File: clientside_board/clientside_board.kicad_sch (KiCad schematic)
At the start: 10 parts, among them J10 Comm Status LED, J11 12V Power Input, J2 USB_B, J4 UART Screw Terminal

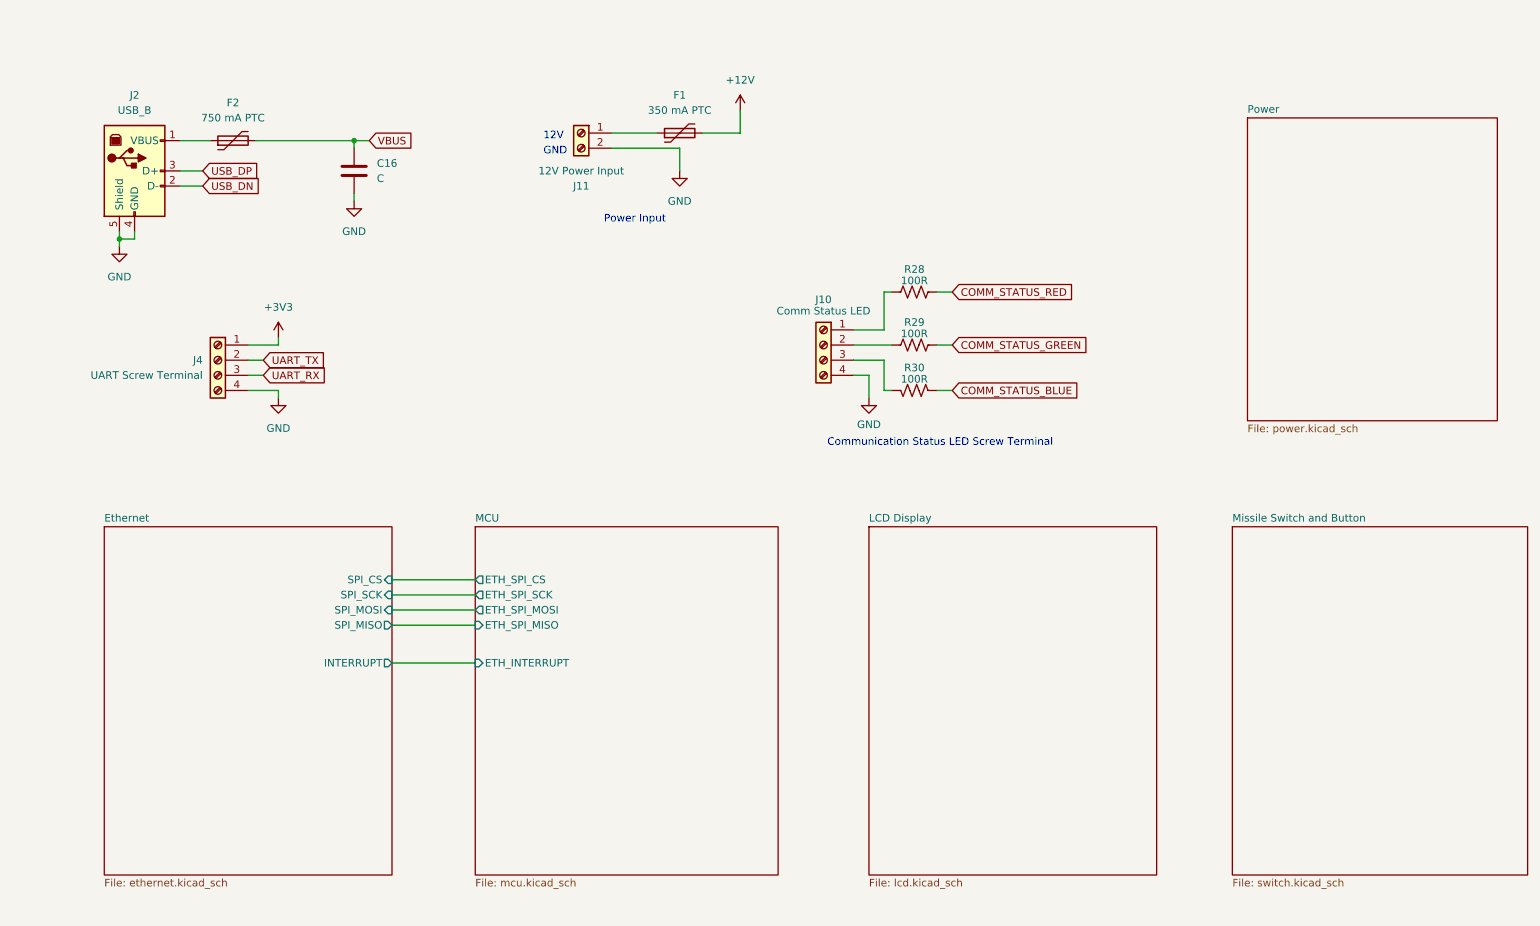
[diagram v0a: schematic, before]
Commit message: Cleanup Power and Ethernet Sheet
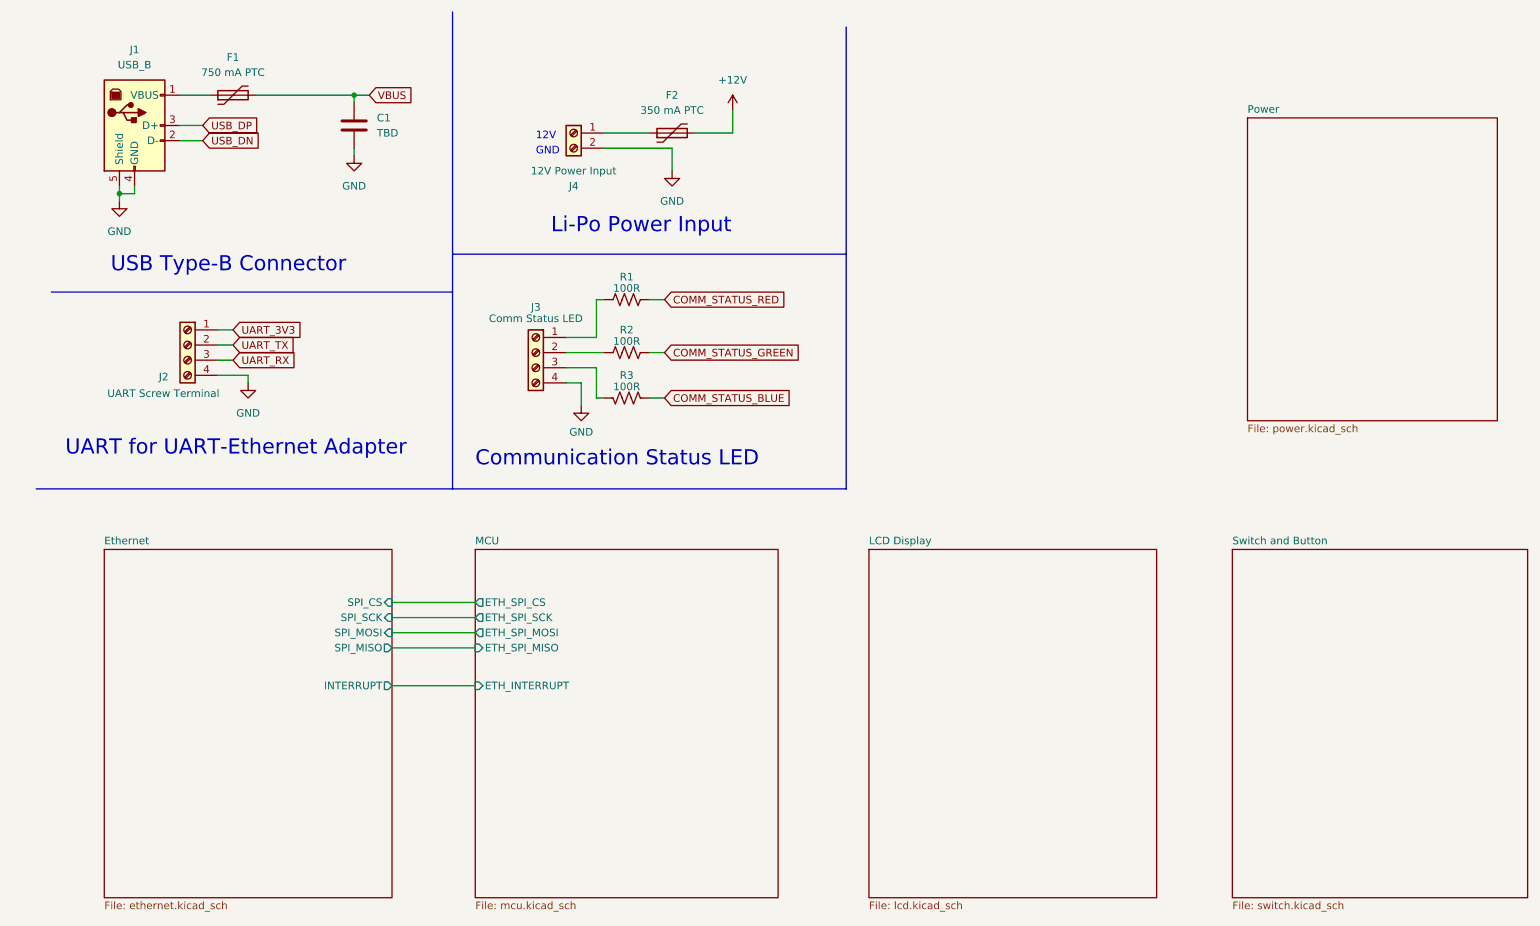
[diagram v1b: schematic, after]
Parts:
- C1: renamed from C16; value C -> TBD; footprint (none) -> Capacitor_SMD:C_0805_2012Metric_Pad1.18x1.45mm_HandSolder
- renumbered F2 to F1, F1 to F2, J2 to J1, J4 to J2, J10 to J3, J11 to J4, R28 to R1, R29 to R2, R30 to R3
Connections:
- net +3V3 renamed UART_3V3
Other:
- sheet Missile Switch and Button renamed Switch and Button
- note added: "Communication Status LED"
- note added: "Li-Po Power Input"
- note added: "UART for UART-Ethernet Adapter"
- note added: "USB Type-B Connector"
- note removed: "Communication Status LED Screw Terminal"
- note removed: "Power Input"
- title: (none) -> Top level connection and connectors
- moved on the sheet: C1, F1, F2, J1, J2, J3, J4, R1, R2, R3

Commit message: Start MCU pin connection
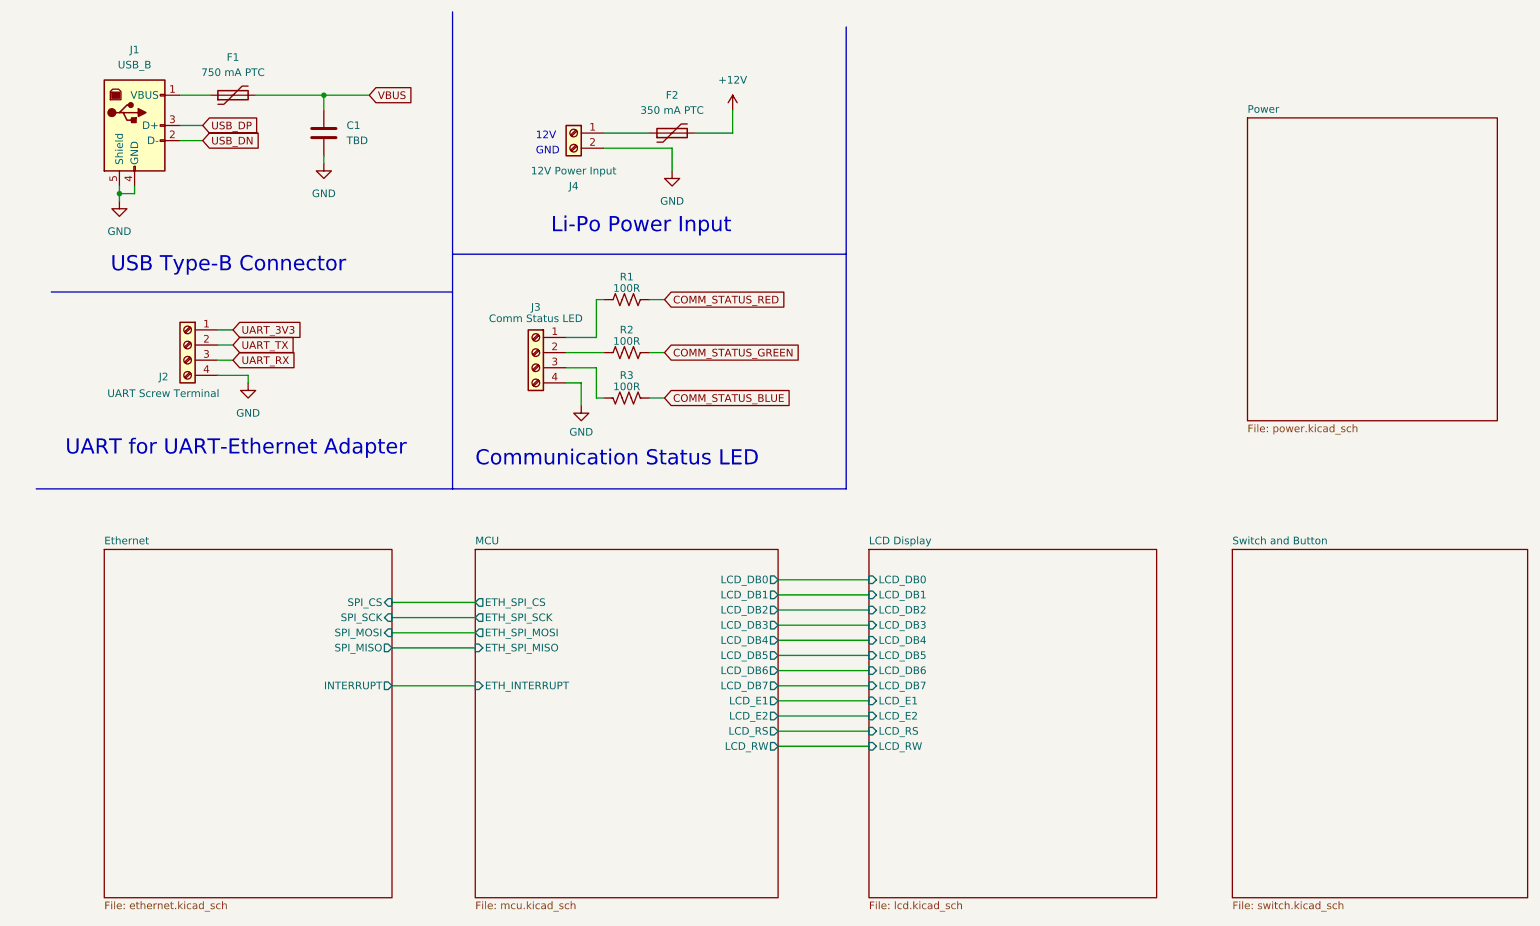
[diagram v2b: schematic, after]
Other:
- sheet LCD Display ports: added LCD_DB0, LCD_DB1, LCD_DB2, LCD_DB3, LCD_DB4, LCD_DB5, LCD_DB6, LCD_DB7, LCD_E1, LCD_E2, LCD_RS, LCD_RW; removed none
- sheet MCU ports: added LCD_DB0, LCD_DB1, LCD_DB2, LCD_DB3, LCD_DB4, LCD_DB5, LCD_DB6, LCD_DB7, LCD_E1, LCD_E2, LCD_RS, LCD_RW; removed none
- moved on the sheet: C1

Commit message: Update power for 5V LCD display
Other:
- sheet Power renamed 3V3 Power
- added sheet 5V Power (5v_power.kicad_sch)
- sheet 3V3 Power: file power.kicad_sch -> 3v3_power.kicad_sch
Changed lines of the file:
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@@
 	)
 	(sheet
-		(at 218.44 30.48)
+		(at 163.83 31.75)
 		(size 41.91 50.8)
 		(exclude_from_sim no)
@@
 			(color 0 0 0 0.0000)
 		)
-		(property "Sheetname" "Power"
-			(at 218.44 29.7684 0)
+		(property "Sheetname" "3V3 Power"
+			(at 163.83 31.0384 0)
 			(effects
 				(font
@@
 			)
 		)
-		(property "Sheetfile" "power.kicad_sch"
-			(at 218.44 81.8646 0)
+		(property "Sheetfile" "3v3_power.kicad_sch"
+			(at 163.83 83.1346 0)
 			(effects
 				(font
@@
 				)
 			)
+		)
+	)
+	(sheet
+		(at 214.63 31.75)
+		(size 40.64 50.8)
+		(exclude_from_sim no)
+		(in_bom yes)
+		(on_board yes)
+		(dnp no)
+		(fields_autoplaced yes)
+		(stroke
+			(width 0.1524)
+			(type solid)
+		)
+		(fill
+			(color 0 0 0 0.0000)
+		)
+		(property "Sheetname" "5V Power"
+			(at 214.63 31.0384 0)
+			(effects
+				(font
+					(size 1.27 1.27)
+				)
+				(justify left bottom)
+			)
+		)
+		(property "Sheetfile" "5v_power.kicad_sch"
+			(at 214.63 83.1346 0)
+			(effects
+				(font
+					(size 1.27 1.27)
+				)
+				(justify left top)
+			)
+		)
+		(instances
+			(project "clientside_board"
+				(path "/94506b77-3097-414f-927c-35c0af27646f"
+					(page "7")
+				)
+			)

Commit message: Top sheet update
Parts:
- C1: footprint Capacitor_SMD:C_0805_2012Metric_Pad1.18x1.45mm_HandSolder -> Capacitor_SMD:C_0603_1608Metric_Pad1.08x0.95mm_HandSolder
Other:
- sheet LCD Display ports: added CTRL_SHIFT_DIR, CTRL_SHIFT_OE, DATA_SHIFT_DIR, DATA_SHIFT_OE; removed none
- sheet MCU ports: added CTRL_SHIFT_DIR, CTRL_SHIFT_OE, DATA_SHIFT_DIR, DATA_SHIFT_OE; removed none
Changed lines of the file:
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@@
+	(wire
+		(pts
+			(xy 139.7 140.97) (xy 154.94 140.97)
+		)
+		(stroke
+			(width 0)
+			(type default)
+		)
+	)
 	(wire
 		(pts
@@
 	(wire
 		(pts
+			(xy 139.7 138.43) (xy 154.94 138.43)
+		)
+		(stroke
+			(width 0)
+			(type default)
+		)
+	)
+	(wire
+		(pts
 			(xy 139.7 115.57) (xy 154.94 115.57)
 		)
@@
 		)
 	)
+	(wire
+		(pts
+			(xy 139.7 146.05) (xy 154.94 146.05)
+		)
+		(stroke
+			(width 0)
+			(type default)
+		)
+	)
 	(polyline
 		(pts
@@
 		(pts
 			(xy 109.22 72.39) (xy 109.22 77.47)
+		)
+		(stroke
+			(width 0)
+			(type default)
+		)
+	)
+	(wire
+		(pts
+			(xy 139.7 143.51) (xy 154.94 143.51)
 		)
 		(stroke
@@
 			)
 		)
-		(property "Footprint" "Capacitor_SMD:C_0805_2012Metric_Pad1.18x1.45mm_HandSolder"
+		(property "Footprint" "Capacitor_SMD:C_0603_1608Metric_Pad1.08x0.95mm_HandSolder"
 			(at 64.4652 36.83 0)
 			(effects
@@
 			)
 		)
+		(pin "CTRL_SHIFT_DIR" input
+			(at 154.94 138.43 180)
+			(effects
+				(font
+					(size 1.27 1.27)
+				)
+				(justify left)
+			)
+		)
+		(pin "CTRL_SHIFT_OE" input
+			(at 154.94 140.97 180)
+			(effects
+				(font
+					(size 1.27 1.27)
+				)
+				(justify left)
+			)
+		)
+		(pin "DATA_SHIFT_DIR" input
+			(at 154.94 143.51 180)
+			(effects
+				(font
+					(size 1.27 1.27)
+				)
+				(justify left)
+			)
+		)
+		(pin "DATA_SHIFT_OE" input
+			(at 154.94 146.05 180)
+			(effects
+				(font
+					(size 1.27 1.27)
+				)
+				(justify left)
+			)
+		)
 		(instances
 			(project "clientside_board"
@@
 			(effects
 				(font
+					(size 1.27 1.27)
+				)
+				(justify right)
+			)
+		)
+		(pin "CTRL_SHIFT_DIR" output
+			(at 139.7 138.43 0)
+			(effects
+				(font
+					(size 1.27 1.27)
+				)
+				(justify right)
+			)
+		)
+		(pin "CTRL_SHIFT_OE" output
+			(at 139.7 140.97 0)
+			(effects
+				(font
+					(size 1.27 1.27)
+				)
+				(justify right)
+			)
+		)
+		(pin "DATA_SHIFT_DIR" output
+			(at 139.7 143.51 0)
+			(effects
+				(font
+					(size 1.27 1.27)
+				)
+				(justify right)
+			)
+		)
+		(pin "DATA_SHIFT_OE" output
+			(at 139.7 146.05 0)
+			(effects
+				(font
